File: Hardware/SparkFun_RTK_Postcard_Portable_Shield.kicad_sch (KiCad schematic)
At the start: 41 parts, among them J1 microSD_Friction, J10 Conn_01x06, J2 Conn_01x05, J4 I2C, J5 Conn_01x04, SW2 Nav Switch, U4 PCA9557PW, U5 OLED_1.3"

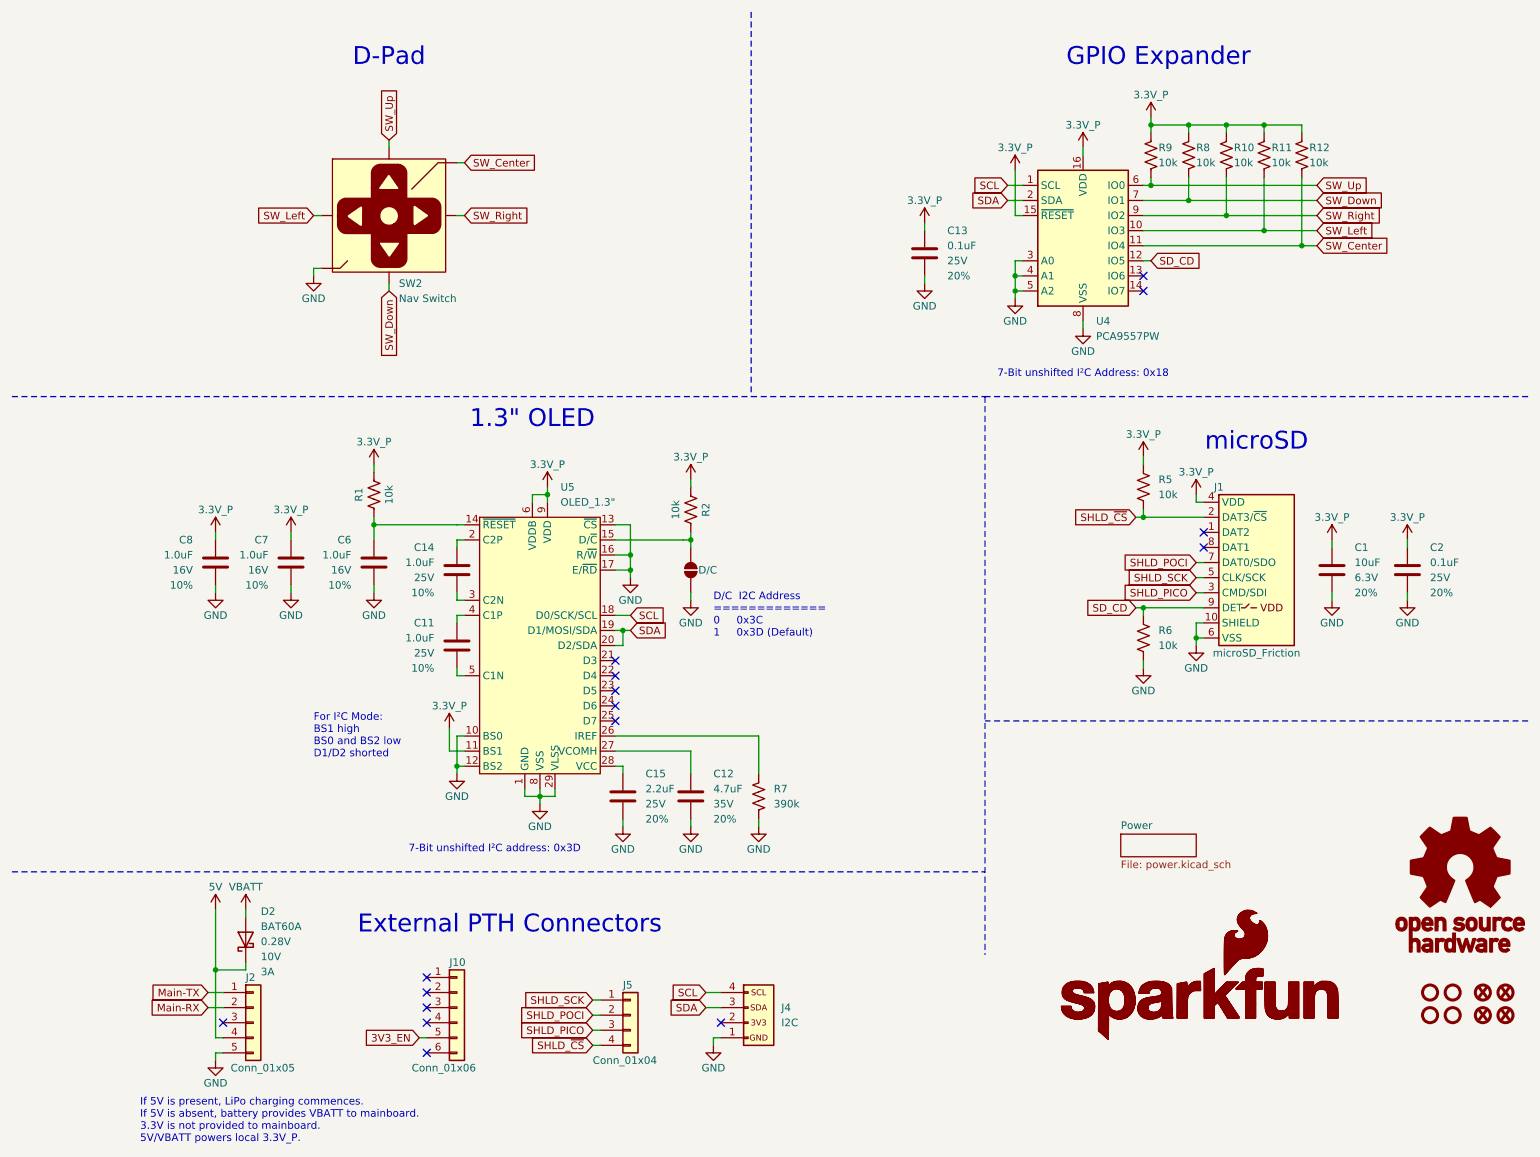
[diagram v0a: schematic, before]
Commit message: Change to dedicated header format.
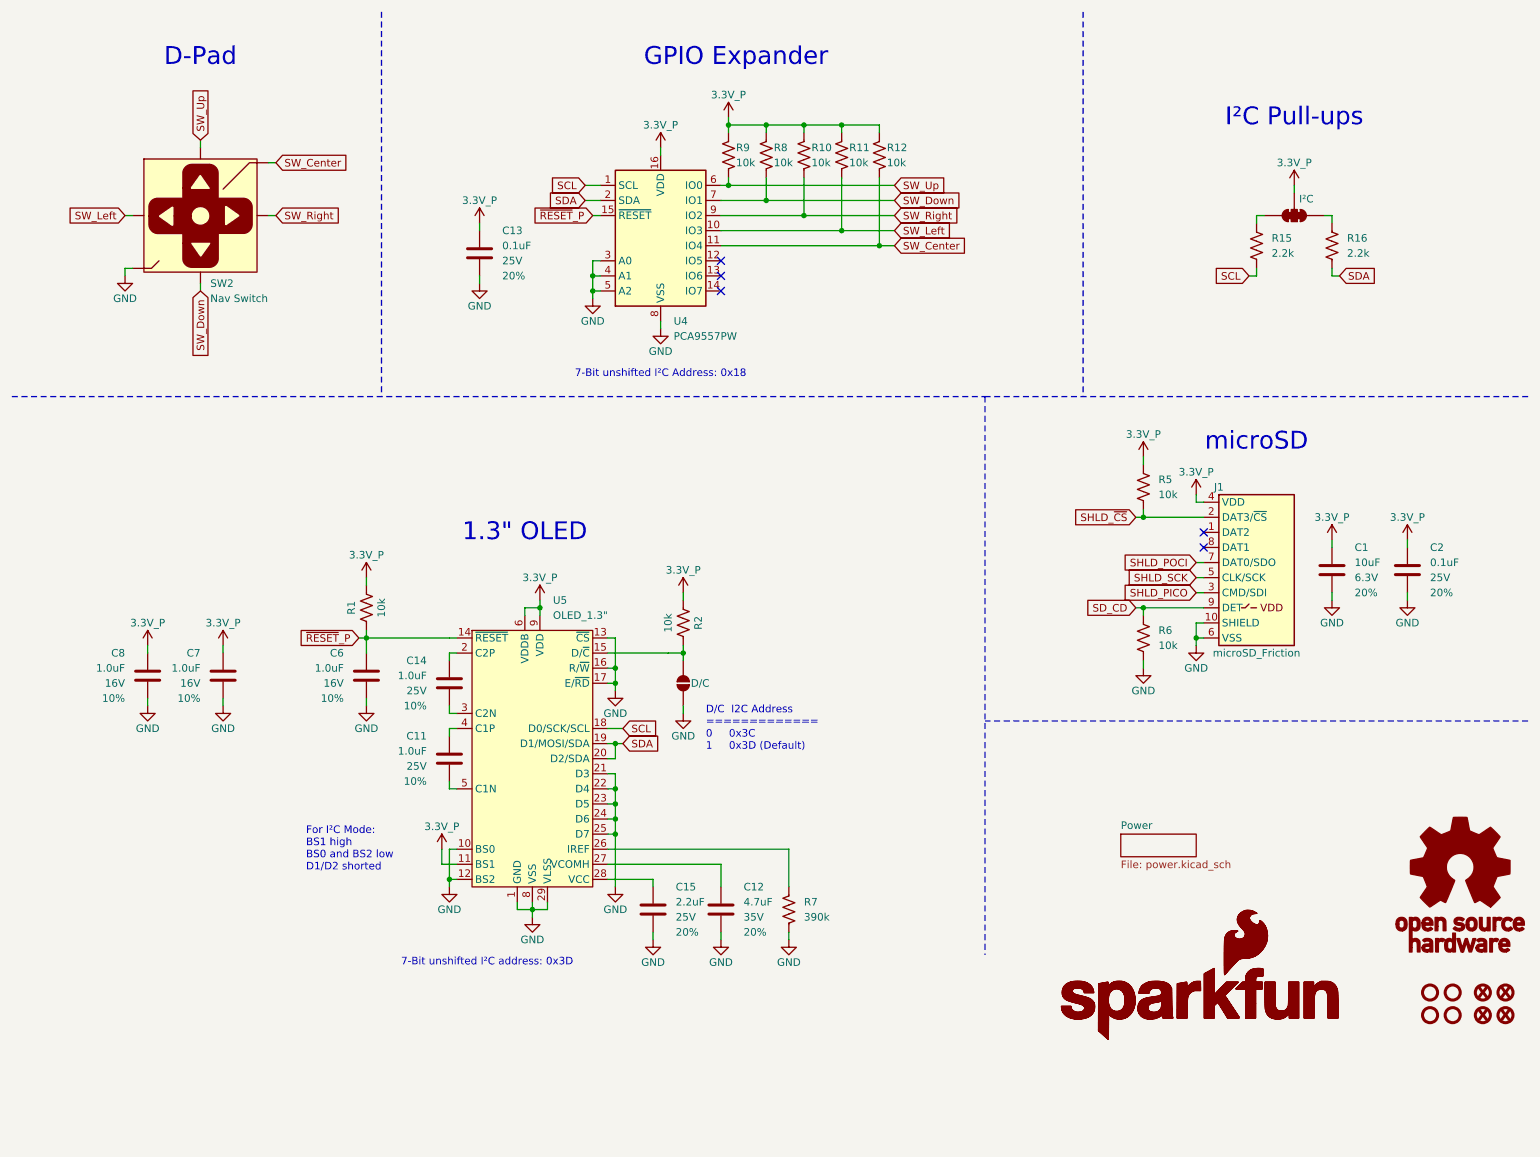
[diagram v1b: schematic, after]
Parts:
- removed D2: BAT60A, SparkFun-Semiconductor-Standard:SOD-323, symbol SparkFun-DiscreteSemi:D_Schottky_3A_10V_0.28V
- removed J10: Conn_01x06, SparkFun-Connector:1x06, symbol SparkFun-Connector:Conn_01x06
- removed J2: Conn_01x05, SparkFun-Connector:1x05, symbol SparkFun-Connector:Conn_01x05
- removed J4: I2C, SparkFun-Connector:1x04, symbol SparkFun-Connector:I2C_01x04
- removed J5: Conn_01x04, SparkFun-Connector:1x04, symbol SparkFun-Connector:Conn_01x04
- added JP4: I²C, SparkFun-Jumper:Jumper_3_NC-2_Trace, symbol SparkFun-Jumper:SolderJumper_3_Bridged123
- added R15, R16: 2.2k, SparkFun-Resistor:R_0603_1608Metric, symbol SparkFun-Resistor:2.2k_0603
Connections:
- net 3.3V_P: now also JP4.2 (C); no longer U4.15 (~{RESET})
- net GND: now also U5.21 (D3), U5.22 (D4), U5.23 (D5), U5.24 (D6), U5.25 (D7)
- net SCL: now also R15.2
- net SDA: now also R16.2
- net SD_CD: no longer U4.12 (IO5)
- net ~{RESET}_P: now reaches C6.1, R1.1, U5.14 (~{RESET})
- net ~{RESET}_P: now also U4.15 (~{RESET})
- new net: JP4.3 (B), R15.1
- new net: JP4.1 (A), R16.1
- no-connect marks 16 -> 5
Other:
- note added: "I²C Pull-ups"
- note removed: "External PTH Connectors"
- note removed: "If 5V is present, LiPo charging commences. If 5V is absent, battery provides VBATT to mainboard. 3.3V is not provided to mainboard. 5V/VBATT powers local 3.3V_P."
- moved on the sheet: C11, C12, C13, C14, C15, C6, C7, C8, R1, R10, R11, R12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
